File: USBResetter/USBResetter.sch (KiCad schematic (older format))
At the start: 13 parts, among them J1 USB In, J2 USB On, J3 USB Out, Q1 BC547, SW1 Bypass, U1 ASSR-1218

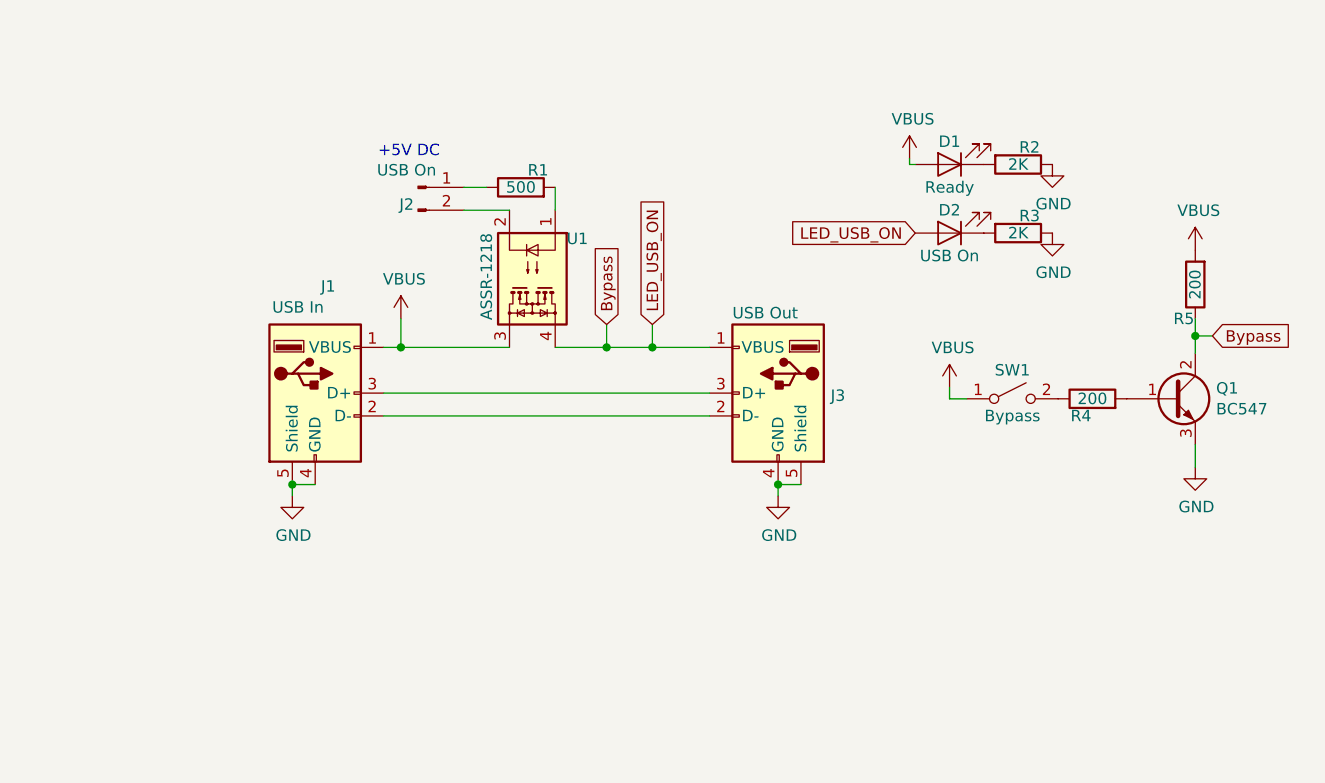
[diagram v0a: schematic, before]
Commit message: Layout Formatting
General layout tidy up.
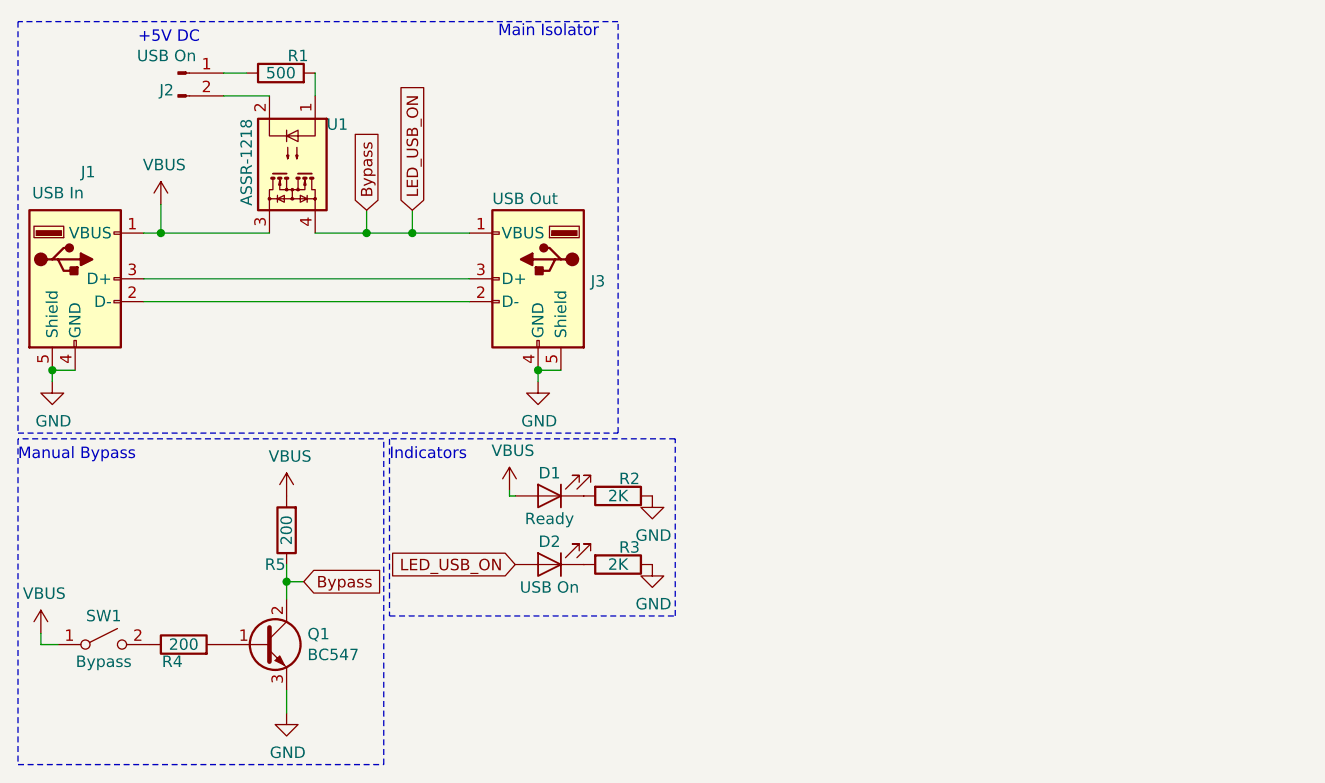
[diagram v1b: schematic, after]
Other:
- note added: "Indicators"
- note added: "Main Isolator"
- note added: "Manual Bypass"
- moved on the sheet: D1, D2, J1, J2, J3, Q1, R1, R2, R3, R4, R5, SW1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

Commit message: PCB Layout, Parts Assignment
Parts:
- D1, D2: footprint (none) -> LEDs:LED_1206
- J1, J3: footprint (none) -> Connectors:USB_A
- J2: footprint (none) -> Pin_Headers:Pin_Header_Straight_1x02_Pitch2.54mm
- Q1: footprint (none) -> TO_SOT_Packages_SMD:SOT-23
- R1, R2, R3, R4, R5: footprint (none) -> Resistors_SMD:R_0805
- SW1: footprint (none) -> Buttons_Switches_SMD:SW_SPST_EVPBF
- U1: footprint Package_SO:SO-4_4.4x4.3mm_P2.54mm -> Housings_SOIC:SO-4_4.4x4.3mm_Pitch2.54mm
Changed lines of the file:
@@
 F 0 "J3" H 2620 1689 50  0000 R CNN
 F 1 "USB Out" H 3050 2050 50  0000 R CNN
-F 2 "" H 3000 1650 50  0001 C CNN
+F 2 "Connectors:USB_A" H 3000 1650 50  0001 C CNN
 F 3 " ~" H 3000 1650 50  0001 C CNN
 	1    2850 1700
@@
 F 0 "U1" V 1600 1350 50  0000 L CNN
 F 1 "ASSR-1218" H 1575 1000 50  0000 L CNN
-F 2 "Package_SO:SO-4_4.4x4.3mm_P2.54mm" H 1575 1000 50  0001 L CIN
+F 2 "Housings_SOIC:SO-4_4.4x4.3mm_Pitch2.54mm" H 1575 1000 50  0001 L CIN
 F 3 "https://docs.broadcom.com/docs/AV02-0173EN" H 1725 1200 50  0001 L CNN
 	1    1775 1200
@@
 F 0 "J2" H 1225 725 50  0000 C CNN
 F 1 "USB On" H 1225 875 50  0000 C CNN
-F 2 "" H 1275 800 50  0001 C CNN
+F 2 "Pin_Headers:Pin_Header_Straight_1x02_Pitch2.54mm" H 1275 800 50  0001 C CNN
 F 3 "~" H 1275 800 50  0001 C CNN
 	1    1275 800
@@
 F 0 "D1" H 2900 2550 50  0000 C CNN
 F 1 "Ready" H 2900 2750 50  0000 C CNN
-F 2 "" H 2900 2650 50  0001 C CNN
+F 2 "LEDs:LED_1206" H 2900 2650 50  0001 C CNN
 F 3 "~" H 2900 2650 50  0001 C CNN
 	1    2900 2650
@@
 F 0 "R2" V 3125 2700 50  0000 C CNN
 F 1 "2K" V 3200 2650 50  0000 C CNN
-F 2 "" V 3130 2650 50  0001 C CNN
+F 2 "Resistors_SMD:R_0805" V 3130 2650 50  0001 C CNN
 F 3 "~" H 3200 2650 50  0001 C CNN
 	1    3200 2650
@@
 F 0 "D2" H 2900 2850 50  0000 C CNN
 F 1 "USB On" H 2900 3050 50  0000 C CNN
-F 2 "" H 2900 2950 50  0001 C CNN
+F 2 "LEDs:LED_1206" H 2900 2950 50  0001 C CNN
 F 3 "~" H 2900 2950 50  0001 C CNN
 	1    2900 2950
@@
 F 0 "R3" V 3125 3000 50  0000 C CNN
 F 1 "2K" V 3200 2950 50  0000 C CNN
-F 2 "" V 3130 2950 50  0001 C CNN
+F 2 "Resistors_SMD:R_0805" V 3130 2950 50  0001 C CNN
 F 3 "~" H 3200 2950 50  0001 C CNN
 	1    3200 2950
@@
 F 0 "Q1" H 1841 3346 50  0000 L CNN
 F 1 "BC547" H 1841 3255 50  0000 L CNN
-F 2 "" H 1850 3400 50  0001 C CNN
+F 2 "TO_SOT_Packages_SMD:SOT-23" H 1850 3400 50  0001 C CNN
 F 3 "~" H 1650 3300 50  0001 C CNN
 	1    1650 3300
@@
 F 0 "SW1" H 950 3425 50  0000 C CNN
 F 1 "Bypass" H 950 3225 50  0000 C CNN
-F 2 "" H 950 3300 50  0001 C CNN
+F 2 "Buttons_Switches_SMD:SW_SPST_EVPBF" H 950 3300 50  0001 C CNN
 F 3 "~" H 950 3300 50  0001 C CNN
 	1    950  3300
@@
 F 0 "R5" H 1800 2950 50  0000 C CNN
 F 1 "200" V 1750 2800 50  0000 C CNN
-F 2 "" V 1680 2800 50  0001 C CNN
+F 2 "Resistors_SMD:R_0805" V 1680 2800 50  0001 C CNN
 F 3 "~" H 1750 2800 50  0001 C CNN
 	1    1750 2800
@@
 F 0 "R4" V 1225 3350 50  0000 C CNN
 F 1 "200" V 1300 3300 50  0000 C CNN
-F 2 "" V 1230 3300 50  0001 C CNN
+F 2 "Resistors_SMD:R_0805" V 1230 3300 50  0001 C CNN
 F 3 "~" H 1300 3300 50  0001 C CNN
 	1    1300 3300
@@
 F 0 "R1" V 1800 725 50  0000 C CNN
 F 1 "500" V 1725 800 50  0000 C CNN
-F 2 "" V 1655 800 50  0001 C CNN
+F 2 "Resistors_SMD:R_0805" V 1655 800 50  0001 C CNN
 F 3 "~" H 1725 800 50  0001 C CNN
 	1    1725 800
@@
 F 0 "J1" H 882 2167 50  0000 C CNN
 F 1 "USB In" H 750 2075 50  0000 C CNN
-F 2 "" H 975 1650 50  0001 C CNN
+F 2 "Connectors:USB_A" H 975 1650 50  0001 C CNN
 F 3 " ~" H 975 1650 50  0001 C CNN
 	1    825  1700

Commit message: Fixed issues with components and layout
Replaced Footprint for NPN Transistor to match the Pinout of the Part. Recreated the Data lines using Differential Pair to ensure optimal USB Data speed and minimal interference.
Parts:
- Q1: symbol Device:Q_NPN_BCE -> Device:Q_NPN_BEC
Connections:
- net Bypass: now also Q1.3 (C); no longer Q1.2 (C)
- net GND: now also Q1.2 (E); no longer Q1.3 (E)
- net USBD-: now reaches J1.2 (D-), J3.2 (D-)
- net USBD+: now reaches J1.3 (D+), J3.3 (D+)
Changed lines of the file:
@@
 	2300 1500 2550 1500
 $Comp
-L Device:Q_NPN_BCE Q1
+L Device:Q_NPN_BEC Q1
 U 1 1 5D050F17
 P 1650 3300
@@
 Text Notes 2200 2500 0    50   ~ 0
 Indicators
+Text Label 1300 1700 0    50   ~ 0
+USBD+
+Text Label 1300 1800 0    50   ~ 0
+USBD-
 $EndSCHEMATC
